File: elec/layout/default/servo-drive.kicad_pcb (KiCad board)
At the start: 4 copper layers, 37.6 x 39.9 mm, 139 parts, among them U37 8Mhz

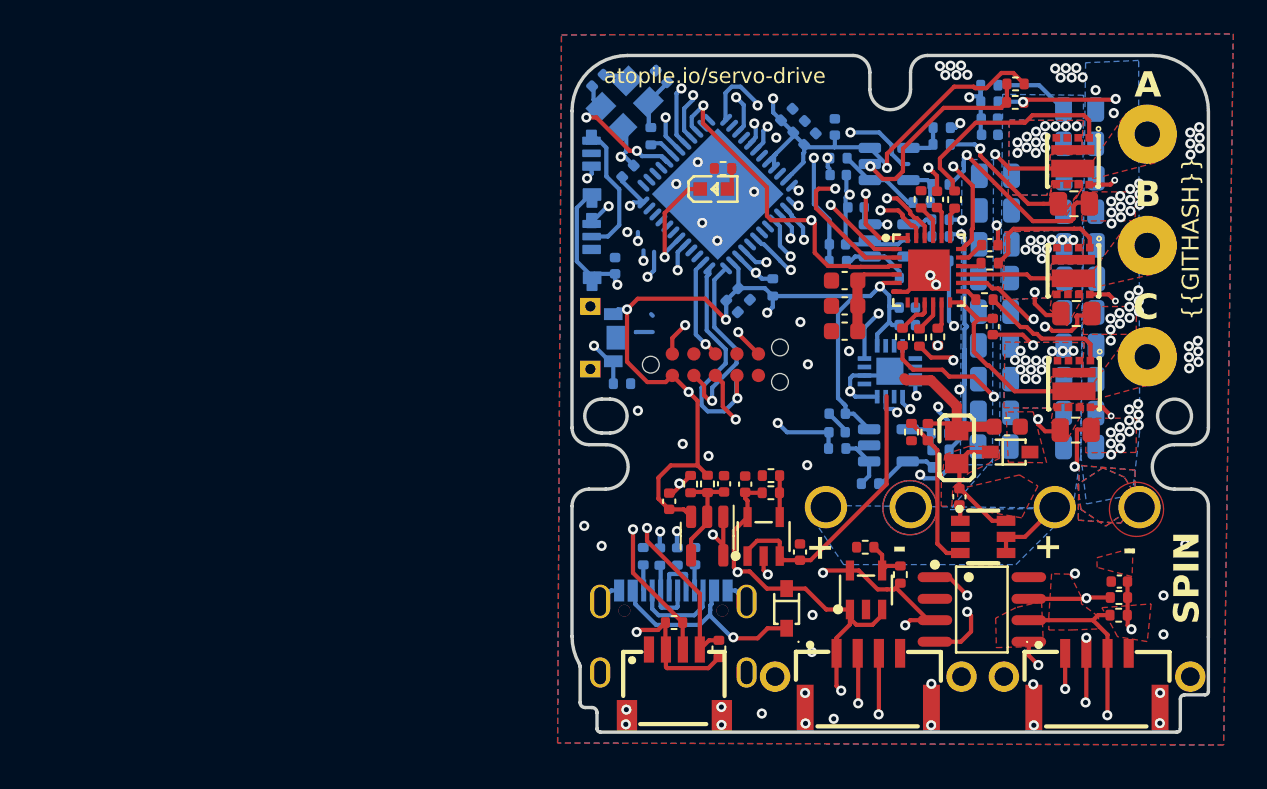
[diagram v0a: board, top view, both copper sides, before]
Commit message: moving layout to correct folder
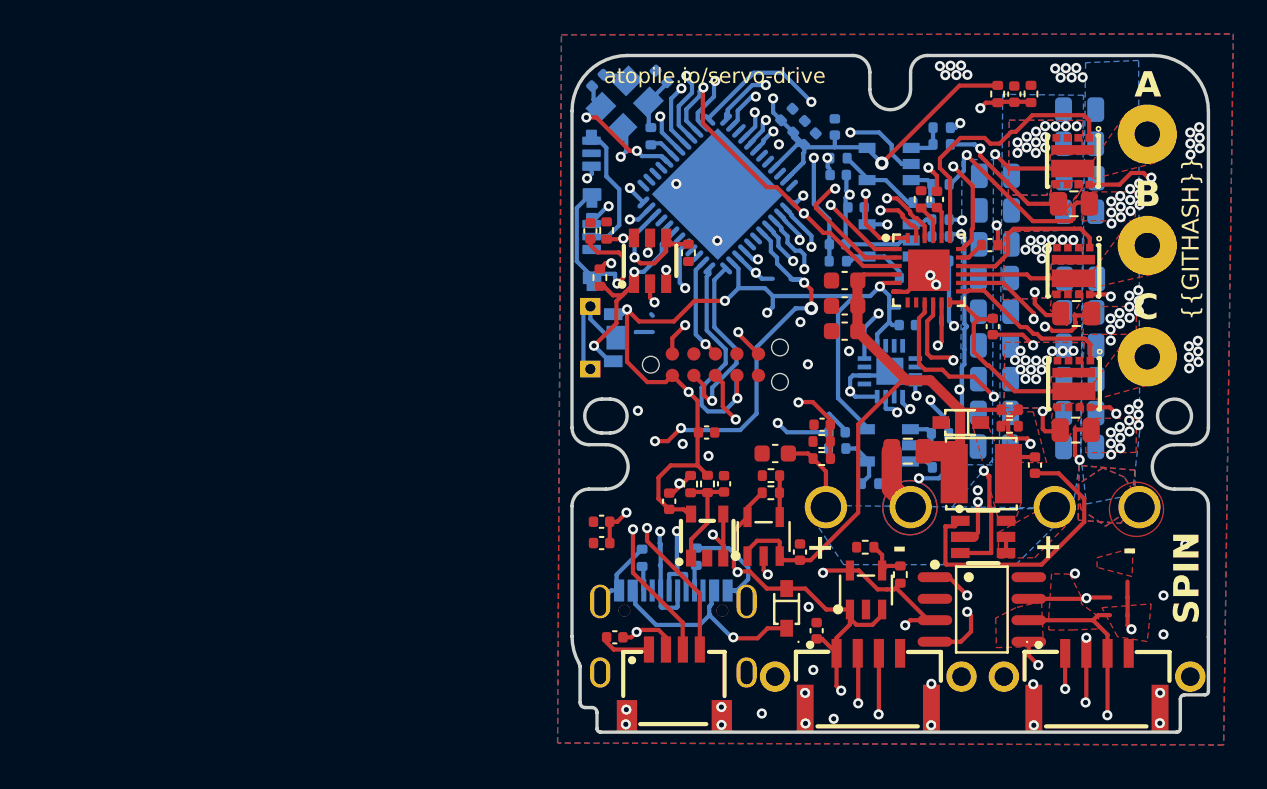
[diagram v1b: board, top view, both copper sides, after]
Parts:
- removed C46: 1uF, Capacitor_SMD:C_0402_1005Metric
- removed C52: 100nF, Capacitor_SMD:C_0402_1005Metric
- removed R23: 60R, Resistor_SMD:R_0402_1005Metric
- removed R24: 1k, Resistor_SMD:R_0402_1005Metric
- removed R27: 10kOhm, Resistor_SMD:R_0402_1005Metric
- removed R28: 1kOhm, Resistor_SMD:R_0402_1005Metric
- removed R32, R33, R34, R35, R36, R37: 10Ohm, Resistor_SMD:R_0402_1005Metric
- removed R39, R40: , Resistor_SMD:R_0402_1005Metric
- C1, C16, C41, C43, C45, C5: value 1uF -> 25V 1uF X5R ±10% 0402 Multilayer Ceramic Capacitors MLCC - SMD/SMT ROHS; footprint Capacitor_SMD:C_0402_1005Metric -> lib:C0402
- C10, C11, C12: value 2200pf -> 50V 2.2nF X7R ±10% 0402 Multilayer Ceramic Capacitors MLCC - SMD/SMT ROHS; footprint Capacitor_SMD:C_0402_1005Metric -> lib:C0402
- C13, C17, C51: value 100nF -> 16V 100nF X7R ±10% 0402 Multilayer Ceramic Capacitors MLCC - SMD/SMT ROHS; footprint Capacitor_SMD:C_0402_1005Metric -> lib:C0402
- C14, C15, C34: value 100nF -> 25V 1uF X5R ±10% 0402 Multilayer Ceramic Capacitors MLCC - SMD/SMT ROHS; footprint Capacitor_SMD:C_0402_1005Metric -> lib:C0402; moved to F.Cu
- C18, C19: value 1uF -> 16V 100nF X7R ±10% 0402 Multilayer Ceramic Capacitors MLCC - SMD/SMT ROHS; footprint Capacitor_SMD:C_0402_1005Metric -> lib:C0402; moved to F.Cu
- C2, C40: value 1uF -> 16V 100nF X7R ±10% 0402 Multilayer Ceramic Capacitors MLCC - SMD/SMT ROHS; footprint Capacitor_SMD:C_0402_1005Metric -> lib:C0402
- C20, C21, C22, C25, C26, C27, C29, C3, C30, C35, C36, C37, C38, C39, C4, C47, C48, C49, C6: value 10uF -> (none); footprint Capacitor_SMD:C_0805_2012Metric -> lib:C0805
- C23, C31, C32: value 4.7uF -> 16V 4.7uF X5R ±10% 0603 Multilayer Ceramic Capacitors MLCC - SMD/SMT ROHS; footprint Capacitor_SMD:C_0603_1608Metric -> lib:C0603
- C24: value 100nF -> 16V 220nF X7R ±10% 0402 Multilayer Ceramic Capacitors MLCC - SMD/SMT ROHS; footprint Capacitor_SMD:C_0402_1005Metric -> lib:C0402
- C28: value 2.2uF -> 16V 100nF X7R ±10% 0402 Multilayer Ceramic Capacitors MLCC - SMD/SMT ROHS; footprint Capacitor_SMD:C_0805_2012Metric -> lib:C0402; moved to F.Cu
- C33: value (none) -> 25V 1uF X5R ±10% 0402 Multilayer Ceramic Capacitors MLCC - SMD/SMT ROHS; footprint Capacitor_SMD:C_0402_1005Metric -> lib:C0402; moved to F.Cu
- C42, C44: value 20pF -> 50V 20pF C0G ±5% 0402 Multilayer Ceramic Capacitors MLCC - SMD/SMT ROHS; footprint Capacitor_SMD:C_0402_1005Metric -> lib:C0402
- C50, C7: value 100nF -> 25V 1uF X5R ±10% 0402 Multilayer Ceramic Capacitors MLCC - SMD/SMT ROHS; footprint Capacitor_SMD:C_0402_1005Metric -> lib:C0402
- C8: value 4.7uF -> 25V 10uF X5R ±10% 0805 Multilayer Ceramic Capacitors MLCC - SMD/SMT ROHS; footprint Capacitor_SMD:C_0603_1608Metric -> lib:C0805
- C9: value 10nF -> 50V 1uF X5R ±10% 0603 Multilayer Ceramic Capacitors MLCC - SMD/SMT ROHS; footprint Capacitor_SMD:C_0402_1005Metric -> lib:C0603
- R1, R38: value 10k -> 62.5mW Thick Film Resistors ±100ppm/℃ ±1% 10kΩ 0402 Chip Resistor - Surface Mount ROHS; footprint Resistor_SMD:R_0402_1005Metric -> lib:R0402
- R10: value 27R -> 62.5mW Thick Film Resistors ±100ppm/℃ ±1% 27.4kΩ 0402 Chip Resistor - Surface Mount ROHS; footprint Resistor_SMD:R_0402_1005Metric -> lib:R0402; moved to F.Cu
- R11: value 1k5 -> 62.5mW ±1% ±200ppm/℃ 3.01kΩ 0402 Chip Resistor - Surface Mount ROHS; footprint Resistor_SMD:R_0402_1005Metric -> lib:R0402; moved to F.Cu
- R12, R14, R26, R45, R49, R51: value 45k -> 62.5mW Thick Film Resistors ±100ppm/℃ ±1% 47kΩ 0402 Chip Resistor - Surface Mount ROHS; footprint Resistor_SMD:R_0402_1005Metric -> lib:R0402
- R13, R25, R44, R48, R50, R6: value 1k -> 62.5mW Thick Film Resistors ±100ppm/℃ ±1% 1kΩ 0402 Chip Resistor - Surface Mount ROHS; footprint Resistor_SMD:R_0402_1005Metric -> lib:R0402
- R15: value 60R -> 62.5mW Thick Film Resistors ±100ppm/℃ ±1% 10kΩ 0402 Chip Resistor - Surface Mount ROHS; footprint Resistor_SMD:R_0402_1005Metric -> lib:R0402
- R16, R46, R52: value 56R -> 62.5mW ±1% ±200ppm/℃ 73.2Ω 0402 Chip Resistor - Surface Mount ROHS; footprint Resistor_SMD:R_0402_1005Metric -> lib:R0402
- R17: value 18k -> 62.5mW Thick Film Resistors ±100ppm/℃ ±1% 20.5kΩ 0402 Chip Resistor - Surface Mount ROHS; footprint Resistor_SMD:R_0402_1005Metric -> lib:R0402
- R18: value 5.1k -> 62.5mW Thick Film Resistors ±100ppm/℃ ±1% 6.34kΩ 0402 Chip Resistor - Surface Mount ROHS; footprint Resistor_SMD:R_0402_1005Metric -> lib:R0402
- R19: value 5.1k -> 10 +/- 0.1 (1%) kiloohm; footprint Resistor_SMD:R_0402_1005Metric -> lib:R0402; moved to F.Cu
- R2: value 10k -> 62.5mW Thick Film Resistors ±100ppm/℃ ±1% 1kΩ 0402 Chip Resistor - Surface Mount ROHS; footprint Resistor_SMD:R_0402_1005Metric -> lib:R0402
- R20: value 5.1k -> 62.5mW Thick Film Resistors ±100ppm/℃ ±1% 10kΩ 0402 Chip Resistor - Surface Mount ROHS; footprint Resistor_SMD:R_0402_1005Metric -> lib:R0402; moved to F.Cu
- R21: value 18k -> 62.5mW Thick Film Resistors ±100ppm/℃ ±1% 11.5kΩ 0402 Chip Resistor - Surface Mount ROHS; footprint Resistor_SMD:R_0402_1005Metric -> lib:R0402
- R22: value 10k -> 62.5mW Thick Film Resistors ±100ppm/℃ ±1% 6.19kΩ 0402 Chip Resistor - Surface Mount ROHS; footprint Resistor_SMD:R_0402_1005Metric -> lib:R0402
- R29: value 147K -> 62.5mW Thick Film Resistors ±100ppm/℃ ±1% 41.2kΩ 0402 Chip Resistor - Surface Mount ROHS; footprint Resistor_SMD:R_0402_1005Metric -> lib:R0402
- R3: value 10k -> 62.5mW Thick Film Resistors ±100ppm/℃ ±1% 100kΩ 0402 Chip Resistor - Surface Mount ROHS; footprint Resistor_SMD:R_0402_1005Metric -> lib:R0402; moved to F.Cu
- R30: value 10K -> 62.5mW Thick Film Resistors ±100ppm/℃ ±1% 4.32kΩ 0402 Chip Resistor - Surface Mount ROHS; footprint Resistor_SMD:R_0402_1005Metric -> lib:R0402
- R31: value 40.2kOhm -> 62.5mW Thick Film Resistors ±100ppm/℃ ±1% 40.2kΩ 0402 Chip Resistor - Surface Mount ROHS; footprint Resistor_SMD:R_0402_1005Metric -> lib:R0402
- R4, R47, R8: value 3mOhm -> (none); footprint Resistor_SMD:R_0805_2012Metric -> lib:R0805
- R5: value 10k_NTC -> 62.5mW Thick Film Resistors ±100ppm/℃ ±1% 5.1kΩ 0402 Chip Resistor - Surface Mount ROHS; footprint Resistor_SMD:R_0402_1005Metric -> lib:R0402; moved to B.Cu
- R7: value 220 -> 62.5mW Thick Film Resistors ±100ppm/℃ ±1% 220Ω 0402 Chip Resistor - Surface Mount ROHS; footprint Resistor_SMD:R_0402_1005Metric -> lib:R0402
- R9: value 27R -> 62.5mW Thick Film Resistors ±100ppm/℃ ±1% 5.1kΩ 0402 Chip Resistor - Surface Mount ROHS; footprint Resistor_SMD:R_0402_1005Metric -> lib:R0402
- U10: footprint lib:L0805 -> lib:IND-SMD_L4.0-W4.0
- U20, U21, U24, U4: footprint Package_TO_SOT_SMD:SOT-23-5 -> lib:SOT-23-5_L3.0-W1.7-P0.95-LS2.8-BR
- U29: footprint lib:LED0603-RD -> lib:SOT-23-6_L2.9-W1.6-P0.95-LS2.8-BR
- U37: value 8Mhz -> (none)
- moved R19 33.7 mm to (232.0, 84.0)
- moved R5 32.8 mm to (212.3, 111.3), turned to 90 degrees
- moved C33 31.0 mm to (219.4, 115.7), turned to 90 degrees
- moved R15 30.6 mm to (230.1, 84.0), turned to -90 degrees
- moved C34 24.5 mm to (206.0, 92.1), turned to 90 degrees
- moved C18 21.9 mm to (207.5, 116.0), turned to 180 degrees
- moved R2 21.7 mm to (211.8, 93.4), turned to -90 degrees
- moved C9 21.7 mm to (216.9, 105.2)
- moved R20 16.6 mm to (206.6, 94.8), turned to -90 degrees
- moved C14 15.9 mm to (206.7, 110.5), turned to 180 degrees
- moved C15 15.9 mm to (206.7, 109.2), turned to 180 degrees
- moved R10 10.3 mm to (219.7, 105.5), turned to 0 degrees
- moved C28 9.73 mm to (231.1, 84.0), turned to 90 degrees
- moved R11 9.54 mm to (219.7, 104.5), turned to 180 degrees
- moved R3 9.08 mm to (207.0, 92.0), turned to 90 degrees
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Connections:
- net SpinServoNEMA17-a_isense renamed power_stage.phase_a.current_sensor-vcc-1
- net SpinServoNEMA17-b_isense renamed power_stage.phase_b.current_sensor-vcc
- net SpinServoNEMA17-data_out renamed ios.led1-vcc
- net SpinServoNEMA17-miso renamed micro-miso
- net SpinServoNEMA17-mosi renamed micro-mosi
- net SpinServoNEMA17-out_a renamed power_stage.phase_a.half_bridge-vcc-2
- net SpinServoNEMA17-out_b renamed power_stage.phase_b.half_bridge-vcc-2
- net SpinServoNEMA17-out_c renamed power_stage.phase_c.half_bridge-vcc-2
- net SpinServoNEMA17-p3 renamed canl
- net SpinServoNEMA17-phase_a renamed power_stage.phase_a-vcc
- net SpinServoNEMA17-phase_b renamed power_stage.phase_b-vcc
- net SpinServoNEMA17-phase_c renamed power_stage.phase_c-vcc
- net SpinServoNEMA17-sck renamed sck
- net SpinServoNEMA17-vin-1 renamed power_stage-vcc-1
- net _a-gnd-2 renamed power_stage.phase_a.half_bridge-gnd
- net _b-i_in-2 renamed power_stage.phase_b.half_bridge-gnd
- net _c-i_in-2 renamed power_stage.phase_c.half_bridge-gnd
- net _i_sense-in-4 renamed power_stage.phase_a.current_sensor.opamp-gnd
- net _i_sense-in-5 renamed power_stage.phase_b.current_sensor.opamp-gnd
- net _i_sense-in_n-5 renamed power_stage.phase_a.current_sensor.opamp-inverting
- net _i_sense-in_n-6 renamed power_stage.phase_b.current_sensor.opamp-inverting
- net _i_sense-in_p-3 renamed power_stage.phase_a.current_sensor.opamp-non_inverting
- net _i_sense-input-10 renamed power_stage.phase_a.current_sensor.bias_div-vcc
- net _i_sense-input-11 renamed power_stage.phase_a.current_sensor.feedback_div-vcc
- net _i_sense-input-12 renamed power_stage.phase_b.current_sensor.feedback_div-vcc
- net _i_sense-input-13 renamed power_stage.phase_c.current_sensor.bias_div-vcc
- net _i_sense-input-14 renamed power_stage.phase_c.current_sensor.feedback_div-vcc
- net _i_sense-out-1 renamed power_stage.phase_c.current_sensor.opamp-gnd
- net _i_sense-output-6 renamed power_stage.phase_b.current_sensor.opamp-non_inverting
- net _i_sense-output-7 renamed power_stage.phase_c.current_sensor.opamp-non_inverting
- net _i_sense-output-8 renamed power_stage.phase_c.current_sensor.opamp-inverting
- net _i_sense-p1-4 renamed power_stage.phase_b.current_sensor.bias_div-vcc
- net gate_reg-cb-1 renamed cb
- net gate_reg-fb renamed power_supply.buck.feedback_div-out
- net gate_reg-sw-1 renamed sw
- net ldo_3v3-adj-1 renamed power_supply.ldo3V3.feedback_div-out
- net ldo_5v-output renamed power_supply.ldo5V.feedback_div-out
- net led2-data_out-1 renamed ios.led2-vcc
- net micro-PA10-2 renamed micro-vcc-4
- net micro-PA13-1 renamed tms
- net micro-PB10-2 renamed pb10
- net micro-PB7-2 renamed micro.micro-sda
- net micro-PC10-2 renamed pc10
- net micro-PC11-2 renamed pc11
- net micro-PC13-2 renamed pc13
- net micro-PC14_OSC32_IN-2 renamed pc14_osc32_in
- net micro-PC15_OSC32_OUT-2 renamed pc15_osc32_out
- net micro-PF1_OSC_OUT-1 renamed pf1_osc_out
- net micro-VBAT-2 renamed micro.micro.ic-vcc
- net micro-in renamed micro.micro.ic-vcc-1
- net micro-out-1 renamed xout
- net micro-rst renamed reset
- net micro-tck renamed tck
- net micro-tdi-1 renamed tdi
- net micro-tdo-1 renamed tdo
- net power_stage-BSTA renamed power_stage.gate_driver.ic-vcc
- net power_stage-BSTB-1 renamed power_stage.gate_driver.ic-vcc-1
- net power_stage-DT-1 renamed power_stage.gate_driver.ic-vcc-3
- net power_stage-bs-1 renamed power_stage.gate_driver.ic-vcc-2
- net power_stage-i_fb_zero-1 renamed power_stage.phase_a.current_sensor-vcc
- net sensor-a-2 renamed position_sensor.ma732-vcc
- net sensor-b-2 renamed position_sensor.ma732-vcc-1
- net sensor-mgh-2 renamed position_sensor.ma732-vcc-3
- net sensor-mgl-2 renamed mgl
- net sensor-nc-2 renamed n_c
- net sensor-pwm-2 renamed pwm
- net sensor-ssck-2 renamed ssck
- net sensor-ssd-2 renamed ssd
- net usbc-vbus-1 renamed power_supply-vcc
- net vref_1V65-vref_unbuf-2 renamed power_stage.voltage_reference.opamp-non_inverting
- C1 pad 1: SpinServoNEMA17-vin -> power_stage-vcc-2
- C1 pad 2: SpinServoNEMA17-gnd -> power_stage-gnd
- C10 pad 2: SpinServoNEMA17-gnd -> power_stage-gnd
- C11 pad 2: SpinServoNEMA17-gnd -> power_stage-gnd
- C12 pad 1: SpinServoNEMA17-c_isense -> power_stage.phase_c.current_sensor-vcc
- C12 pad 2: SpinServoNEMA17-gnd -> power_stage-gnd
- C13 pad 1: SpinServoNEMA17-vin -> power_stage-vcc-2
- C13 pad 2: SpinServoNEMA17-gnd -> power_stage-gnd
- C14 pad 1: SpinServoNEMA17-vin -> power_supply-vcc-1
- C14 pad 2: SpinServoNEMA17-gnd -> power_stage-gnd
- C15 pad 1: SpinServoNEMA17-vin -> power_supply-vcc-1
- C15 pad 2: SpinServoNEMA17-gnd -> power_stage-gnd
- C16 pad 1: SpinServoNEMA17-p1 -> power_stage-vcc-2
- C16 pad 2: SpinServoNEMA17-gnd -> power_stage-gnd
- C17 pad 1: SpinServoNEMA17-vin -> power_stage-vcc-2
- C17 pad 2: SpinServoNEMA17-gnd -> power_stage-gnd
- C18 pad 1: SpinServoNEMA17-p1 -> power_stage-vcc-2
- C18 pad 2: SpinServoNEMA17-gnd -> power_stage-gnd
- C19 pad 1: SpinServoNEMA17-vin -> micro-vcc-3
- C19 pad 2: SpinServoNEMA17-gnd -> power_stage-gnd
- C2 pad 2: SpinServoNEMA17-gnd -> power_stage-gnd
- C20 pad 1: SpinServoNEMA17-vin-2 -> power_stage-vcc
- C20 pad 2: SpinServoNEMA17-gnd -> power_stage-gnd
- C21 pad 1: SpinServoNEMA17-vin-2 -> power_stage-vcc
- C21 pad 2: SpinServoNEMA17-gnd -> power_stage-gnd
- C22 pad 1: SpinServoNEMA17-vin-2 -> power_stage-vcc
- C22 pad 2: SpinServoNEMA17-gnd -> power_stage-gnd
- C23 pad 2: SpinServoNEMA17-gnd -> power_stage-gnd
- C25 pad 1: SpinServoNEMA17-vin-2 -> power_stage-vcc
- C25 pad 2: SpinServoNEMA17-gnd -> power_stage-gnd
- C26 pad 1: SpinServoNEMA17-vin-2 -> power_stage-vcc
- C26 pad 2: SpinServoNEMA17-gnd -> power_stage-gnd
- C27 pad 1: SpinServoNEMA17-vin-2 -> power_stage-vcc
- C27 pad 2: SpinServoNEMA17-gnd -> power_stage-gnd
- C28 pad 1: SpinServoNEMA17-vin-2 -> micro-vcc-2
- C28 pad 2: SpinServoNEMA17-gnd -> power_stage-gnd
- C29 pad 1: SpinServoNEMA17-vin-2 -> power_stage-vcc
- C29 pad 2: SpinServoNEMA17-gnd -> power_stage-gnd
- C3 pad 1: SpinServoNEMA17-vin-2 -> power_stage-vcc
- C3 pad 2: SpinServoNEMA17-gnd -> power_stage-gnd
- C30 pad 1: SpinServoNEMA17-vin-2 -> power_stage-vcc
- C30 pad 2: SpinServoNEMA17-gnd -> power_stage-gnd
- C31 pad 2: SpinServoNEMA17-gnd -> power_stage-gnd
- C32 pad 2: SpinServoNEMA17-gnd -> power_stage-gnd
- C33 pad 1: SpinServoNEMA17-vin_sense -> power_supply-vcc-1
- C33 pad 2: SpinServoNEMA17-gnd -> power_stage-gnd
- C34 pad 1: SpinServoNEMA17-vin_sense -> power_supply-vcc-1
- C34 pad 2: SpinServoNEMA17-gnd -> power_stage-gnd
- C35 pad 1: SpinServoNEMA17-vin-2 -> power_stage-vcc
- C35 pad 2: SpinServoNEMA17-gnd -> power_stage-gnd
- C36 pad 1: SpinServoNEMA17-vin-2 -> power_stage-vcc
- C36 pad 2: SpinServoNEMA17-gnd -> power_stage-gnd
- C37 pad 1: SpinServoNEMA17-vin-2 -> power_stage-vcc
- C37 pad 2: SpinServoNEMA17-gnd -> power_stage-gnd
- C38 pad 1: SpinServoNEMA17-vin-2 -> power_stage-vcc
- C38 pad 2: SpinServoNEMA17-gnd -> power_stage-gnd
- C39 pad 1: SpinServoNEMA17-vin-2 -> power_stage-vcc
- C39 pad 2: SpinServoNEMA17-gnd -> power_stage-gnd
- C4 pad 1: SpinServoNEMA17-vin-2 -> power_stage-vcc
- C4 pad 2: SpinServoNEMA17-gnd -> power_stage-gnd
- C40 pad 1: SpinServoNEMA17-vin -> power_stage-vcc-2
- C40 pad 2: SpinServoNEMA17-gnd -> power_stage-gnd
- C42 pad 2: SpinServoNEMA17-gnd -> power_stage-gnd
- C44 pad 2: SpinServoNEMA17-gnd -> power_stage-gnd
- C47 pad 1: SpinServoNEMA17-vin-2 -> power_stage-vcc
- C47 pad 2: SpinServoNEMA17-gnd -> power_stage-gnd
- C48 pad 1: SpinServoNEMA17-vin-2 -> power_stage-vcc
- C48 pad 2: SpinServoNEMA17-gnd -> power_stage-gnd
- C49 pad 1: SpinServoNEMA17-vin-2 -> power_stage-vcc
- C49 pad 2: SpinServoNEMA17-gnd -> power_stage-gnd
- C5 pad 2: SpinServoNEMA17-gnd -> power_stage-gnd
- C50 pad 1: SpinServoNEMA17-vin -> power_stage-vcc-2
- C50 pad 2: SpinServoNEMA17-gnd -> power_stage-gnd
- C51 pad 1: SpinServoNEMA17-vin -> power_stage-vcc-2
- C51 pad 2: SpinServoNEMA17-gnd -> power_stage-gnd
- C6 pad 1: SpinServoNEMA17-vin-2 -> power_stage-vcc
- C6 pad 2: SpinServoNEMA17-gnd -> power_stage-gnd
- C7 pad 1: SpinServoNEMA17-vin -> power_stage-vcc-2
- C7 pad 2: SpinServoNEMA17-gnd -> power_stage-gnd
- C8 pad 2: SpinServoNEMA17-gnd -> power_stage-gnd
- C9 pad 1: canbus-v_mid-2 -> power_stage-vcc
- C9 pad 2: SpinServoNEMA17-gnd -> power_stage-gnd
- J1 pad 1: SpinServoNEMA17-gnd -> power_stage-gnd
- J1 pad 2: SpinServoNEMA17-gnd -> power_stage-gnd
- J1 pad 3: SpinServoNEMA17-gnd -> power_stage-gnd
- J1 pad 4: SpinServoNEMA17-gnd -> power_stage-gnd
- J1 pad A1: SpinServoNEMA17-gnd -> power_stage-gnd
- J1 pad A12: SpinServoNEMA17-gnd -> power_stage-gnd
- J1 pad A5: SpinServoNEMA17-cc1 -> cc1
- J1 pad A6: SpinServoNEMA17-dp -> dp
- J1 pad A7: SpinServoNEMA17-dm -> dm
- J1 pad A8: usbc-sbu-1 -> sub1
- J1 pad B1: SpinServoNEMA17-gnd -> power_stage-gnd
- J1 pad B12: SpinServoNEMA17-gnd -> power_stage-gnd
- J1 pad B5: SpinServoNEMA17-cc2 -> cc2
- J1 pad B6: SpinServoNEMA17-dp -> dp
- J1 pad B7: SpinServoNEMA17-dm -> dm
- J1 pad B8: usbc-sbu-1 -> sub2
- R1 pad 1: SpinServoNEMA17-vin -> power_stage-vcc-2
- R10 pad 1: micro-PA11-1 -> power_stage-vcc
- R10 pad 2: SpinServoNEMA17-dm -> micro-vcc-3
- R11 pad 1: micro-PA12-1 -> micro-vcc-3
- R11 pad 2: SpinServoNEMA17-vin -> power_stage-gnd
- R15 pad 1: SpinServoNEMA17-p2 -> power_stage-vcc-2
- R15 pad 2: canbus-v_mid-2 -> micro-vcc-2
- R17 pad 1: SpinServoNEMA17-p1 -> power_supply-vcc-1
- R18 pad 2: SpinServoNEMA17-gnd -> power_stage-gnd
- R19 pad 1: SpinServoNEMA17-cc1 -> micro-vcc-2
- R19 pad 2: SpinServoNEMA17-gnd -> power_stage-gnd
- R2 pad 1: SpinServoNEMA17-vin -> micro.micro-io
- R2 pad 2: SpinServoNEMA17-temp_sense -> power_stage-gnd
- R20 pad 1: SpinServoNEMA17-cc2 -> power_stage-gnd
- R20 pad 2: SpinServoNEMA17-gnd -> micro-vcc-1
- R21 pad 1: SpinServoNEMA17-vin -> power_stage-vcc-2
- R22 pad 2: SpinServoNEMA17-gnd -> power_stage-gnd
- R3 pad 1: SpinServoNEMA17-gnd -> micro.micro-io-1
- R3 pad 2: SpinServoNEMA17-in -> power_stage-gnd
- R30 pad 2: SpinServoNEMA17-gnd -> power_stage-gnd
- R31 pad 2: SpinServoNEMA17-gnd -> power_stage-gnd
- R38 pad 2: SpinServoNEMA17-gnd -> power_stage-gnd
- R4 pad 2: SpinServoNEMA17-gnd -> power_stage-gnd
- R47 pad 2: SpinServoNEMA17-gnd -> power_stage-gnd
- R5 pad 1: SpinServoNEMA17-temp_sense -> cc1
- R5 pad 2: SpinServoNEMA17-gnd -> power_stage-gnd
- R52 pad 2: SpinServoNEMA17-c_isense -> power_stage.phase_c.current_sensor-vcc
- R8 pad 2: SpinServoNEMA17-gnd -> power_stage-gnd
- R9 pad 1: micro-PA12-1 -> cc2
- R9 pad 2: SpinServoNEMA17-dp -> power_stage-gnd
- U1 pad 1: _b-high_gate-2 -> power_stage.phase_b.half_bridge-vcc
- U1 pad 10: SpinServoNEMA17-vin-2 -> power_stage-vcc
- U1 pad 2: SpinServoNEMA17-vin-2 -> power_stage-vcc
- U1 pad 3: SpinServoNEMA17-vin-2 -> power_stage-vcc
- U1 pad 4: SpinServoNEMA17-vin-2 -> power_stage-vcc
- U1 pad 8: _b-low_gate-2 -> power_stage.phase_b.half_bridge-vcc-1
- U11 pad 1: SpinServoNEMA17-in -> micro-vcc-1
- U11 pad 2: SpinServoNEMA17-vin -> power_stage-vcc-2
- U11 pad 3: (no net) -> anchor
- U11 pad 4: (no net) -> anchor
- U12 pad 10: power_stage-GLB-1 -> power_stage.phase_b.half_bridge-vcc-1
- U12 pad 11: power_stage-GLA-1 -> power_stage.phase_a.half_bridge-vcc-1
- U12 pad 13: power_stage-GHC-1 -> power_stage.phase_c.half_bridge-vcc
- U12 pad 16: power_stage-GHB-1 -> power_stage.phase_b.half_bridge-vcc
- U12 pad 19: power_stage-GHA-1 -> power_stage.phase_a.half_bridge-vcc
- U12 pad 25: SpinServoNEMA17-gnd -> power_stage-gnd
- U12 pad 5: SpinServoNEMA17-vin -> power_stage-vcc-2
- U12 pad 6: SpinServoNEMA17-gnd -> power_stage-gnd
- U12 pad 7: drv8300-NC2-2 -> (no net)
- U12 pad 8: drv8300-NC1-2 -> (no net)
- U12 pad 9: power_stage-GLC-1 -> power_stage.phase_c.half_bridge-vcc-1
- U13 pad 11: SpinServoNEMA17-enable -> power_stage.phase_c.current_sensor-vcc
- U13 pad 12: micro-PA4-2 -> micro-vcc-2
- U13 pad 13: SpinServoNEMA17-in -> micro-vcc-3
- U13 pad 14: micro-PA6-2 -> micro.micro-io-1
- U13 pad 15: SpinServoNEMA17-led_pixel -> micro.micro-mosi
- U13 pad 16: micro-PC4-2 -> scl
- U13 pad 19: SpinServoNEMA17-c_isense -> pb2
- U13 pad 20: SpinServoNEMA17-vin -> (no net)
- U13 pad 21: SpinServoNEMA17-vin -> power_stage-vcc-2
- U13 pad 23: SpinServoNEMA17-vin -> power_stage-vcc-2
- U13 pad 24: SpinServoNEMA17-cs -> pb11
- U13 pad 25: SpinServoNEMA17-vin_sense -> cs
- U13 pad 29: micro-PC6-2 -> micro-vcc
- U13 pad 30: micro-PA8-2 -> micro-sda
- U13 pad 31: SpinServoNEMA17-temp_sense -> pa9
- U13 pad 33: micro-PA11-1 -> dm
- U13 pad 34: micro-PA12-1 -> dp
- U13 pad 35: SpinServoNEMA17-vin -> power_stage-vcc-2
- U13 pad 42: micro-PB4 -> micro.micro-miso
- U13 pad 43: micro-rx -> micro-vcc-1
- U13 pad 44: micro-tx -> pb6
- U13 pad 46: SpinServoNEMA17-scl -> micro.micro-io
- U13 pad 47: SpinServoNEMA17-sda -> tx
- U13 pad 48: SpinServoNEMA17-vin -> power_stage-vcc-2
- U13 pad 49: SpinServoNEMA17-gnd -> power_stage-gnd
- U14 pad 1: SpinServoNEMA17-gnd -> power_stage-gnd
- U14 pad 2: SpinServoNEMA17-vin-2 -> power_stage-vcc
- U14 pad 3: (no net) -> power_stage-gnd
- U14 pad 4: (no net) -> power_stage-gnd
- U15 pad 1: SpinServoNEMA17-gnd -> power_stage-gnd
- U15 pad 2: SpinServoNEMA17-vin -> power_stage-vcc-2
- U15 pad 3: SpinServoNEMA17-sda -> micro-sda
- U15 pad 4: SpinServoNEMA17-scl -> scl
- U15 pad 5: (no net) -> power_stage-gnd
- U15 pad 6: (no net) -> power_stage-gnd
- U16 pad 1: SpinServoNEMA17-vin -> power_stage-vcc-2
- U16 pad 3: SpinServoNEMA17-gnd -> power_stage-gnd
- U16 pad 5: SpinServoNEMA17-gnd -> power_stage-gnd
- U18 pad 10: SpinServoNEMA17-gnd -> power_stage-gnd
- U18 pad 13: SpinServoNEMA17-vin -> power_stage-vcc-2
- U18 pad 17: SpinServoNEMA17-gnd -> power_stage-gnd
- U18 pad 3: (no net) -> position_sensor.ma732-vcc-2
- U18 pad 5: SpinServoNEMA17-cs -> cs
- U18 pad 8: SpinServoNEMA17-gnd -> power_stage-gnd
- U19 pad 2: SpinServoNEMA17-gnd -> power_stage-gnd
- U2 pad 1: SpinServoNEMA17-gnd -> power_stage-gnd
- U2 pad 2: SpinServoNEMA17-vin-2 -> power_stage-vcc
- U2 pad 3: (no net) -> power_stage-gnd
- U2 pad 4: (no net) -> power_stage-gnd
- U20 pad 2: SpinServoNEMA17-gnd -> power_stage-gnd
- U20 pad 5: SpinServoNEMA17-vin -> power_stage-vcc-2
- U21 pad 2: SpinServoNEMA17-gnd -> power_stage-gnd
- U21 pad 5: SpinServoNEMA17-vin -> power_stage-vcc-2
- U22 pad 2: SpinServoNEMA17-gnd -> power_stage-gnd
- U22 pad 5: SpinServoNEMA17-p1 -> power_supply-vcc-1
- U23 pad 1: SpinServoNEMA17-p1 -> power_supply-vcc-1
- U23 pad 2: SpinServoNEMA17-gnd -> power_stage-gnd
- U23 pad 3: SpinServoNEMA17-p1 -> power_supply-vcc-1
- U23 pad 5: SpinServoNEMA17-vin -> power_stage-vcc-2
- U24 pad 2: SpinServoNEMA17-gnd -> power_stage-gnd
- U24 pad 5: SpinServoNEMA17-vin -> power_stage-vcc-2
- U25 pad 1: micro-tx -> tx
- U25 pad 2: SpinServoNEMA17-gnd -> power_stage-gnd
- U25 pad 3: SpinServoNEMA17-vin -> power_stage-vcc-2
- U25 pad 4: micro-rx -> rx
- U25 pad 5: canbus-v_mid-2 -> vref
- U25 pad 7: SpinServoNEMA17-p2 -> canh
- U25 pad 8: SpinServoNEMA17-gnd -> power_stage-gnd
- U26 pad 1: SpinServoNEMA17-p1 -> power_supply-vcc-1
- U26 pad 2: SpinServoNEMA17-p2 -> canh
- U26 pad 4: SpinServoNEMA17-gnd -> power_stage-gnd
- U26 pad 5: (no net) -> power_stage-gnd
- U26 pad 6: (no net) -> power_stage-gnd
- U27 pad 1: SpinServoNEMA17-p1 -> power_supply-vcc-1
- U27 pad 2: SpinServoNEMA17-p2 -> canh
- U27 pad 4: SpinServoNEMA17-gnd -> power_stage-gnd
- U27 pad 5: (no net) -> power_stage-gnd
- U27 pad 6: (no net) -> power_stage-gnd
- U28 pad 1: _a-high_gate-2 -> power_stage.phase_a.half_bridge-vcc
- U28 pad 10: SpinServoNEMA17-vin-2 -> power_stage-vcc
- U28 pad 2: SpinServoNEMA17-vin-2 -> power_stage-vcc
- U28 pad 3: SpinServoNEMA17-vin-2 -> power_stage-vcc
- U28 pad 4: SpinServoNEMA17-vin-2 -> power_stage-vcc
- U28 pad 8: _a-low_gate-2 -> power_stage.phase_a.half_bridge-vcc-1
- U29 pad 1: micro-PB4 -> micro-vcc-1
- U29 pad 2: debug_led_1-A-2 -> power_stage-gnd
- U3 pad 1: _c-high_gate-2 -> power_stage.phase_c.half_bridge-vcc
- U3 pad 10: SpinServoNEMA17-vin-2 -> power_stage-vcc
- U3 pad 2: SpinServoNEMA17-vin-2 -> power_stage-vcc
- U3 pad 3: SpinServoNEMA17-vin-2 -> power_stage-vcc
- U3 pad 4: SpinServoNEMA17-vin-2 -> power_stage-vcc
- U3 pad 8: _c-low_gate-2 -> power_stage.phase_c.half_bridge-vcc-1
- U30 pad 1: SpinServoNEMA17-p1 -> power_supply-vcc-1
- U32 pad 1: SpinServoNEMA17-p1 -> power_supply-vcc-1
- U32 pad 2: SpinServoNEMA17-gnd -> power_stage-gnd
- U33 pad 2: SpinServoNEMA17-gnd -> power_stage-gnd
- U35 pad 2: SpinServoNEMA17-gnd -> power_stage-gnd
- U36 pad 2: SpinServoNEMA17-gnd -> power_stage-gnd
- U37 pad 2: SpinServoNEMA17-gnd -> power_stage-gnd
- U37 pad 4: SpinServoNEMA17-gnd -> power_stage-gnd
- U4 pad 2: SpinServoNEMA17-gnd -> power_stage-gnd
- U4 pad 5: SpinServoNEMA17-vin -> power_stage-vcc-2
- U5 pad 1: SpinServoNEMA17-p1 -> power_supply-vcc-1
- U5 pad 2: SpinServoNEMA17-gnd -> power_stage-gnd
- U5 pad 4: SpinServoNEMA17-led_pixel -> micro-vcc
- U6 pad 2: SpinServoNEMA17-gnd -> power_stage-gnd
- U6 pad 4: SpinServoNEMA17-vin-2 -> power_stage-vcc
- U6 pad 5: SpinServoNEMA17-vin-2 -> power_stage-vcc
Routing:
- net SpinServoNEMA17-vin: track 114.6 -> 0.00 mm, vias 13 -> 0
- net power_stage-vcc-2: track 0.00 -> 111.3 mm, vias 0 -> 15
- net power_supply-vcc-1: track 0.00 -> 77.8 mm, vias 0 -> 5
- net SpinServoNEMA17-p1: track 70.9 -> 0.00 mm, vias 4 -> 0
- net power_stage-gnd: track 0.00 -> 56.3 mm, vias 0 -> 88
- net SpinServoNEMA17-gnd: track 44.5 -> 0.00 mm, vias 106 -> 0
- net tx: track 0.00 -> 38.2 mm, vias 0 -> 2
- net scl: track 0.00 -> 37.5 mm, vias 0 -> 2
- net micro-sda: track 0.00 -> 36.5 mm, vias 0 -> 5
- net micro-rx: track 35.8 -> 0.00 mm, vias 2 -> 0
- net rx: track 0.00 -> 34.9 mm, vias 0 -> 2
- net micro-tx: track 33.9 -> 0.00 mm, vias 2 -> 0
- net SpinServoNEMA17-in: track 32.4 -> 0.00 mm, vias 2 -> 0
- net power_stage.phase_c.current_sensor-vcc: track 0.00 -> 30.7 mm, vias 0 -> 3
- net SpinServoNEMA17-scl: track 29.6 -> 0.00 mm, vias 2 -> 0
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- added copper zone on B.Cu, net power_stage-gnd
- added copper zone on F.Cu, net power_stage-gnd
- added copper zone on In1.Cu, net power_stage-gnd
- added copper zone on In2.Cu, net power_stage-gnd
- added copper zone on B.Cu, net power_stage-vcc
- added copper zone on F.Cu, net power_stage-vcc
- added copper zone on In1.Cu, net power_stage-vcc
- added copper zone on In2.Cu, net power_stage-vcc
- added copper zone on In2.Cu, net power_stage-vcc-2
- removed copper zone on B.Cu, net SpinServoNEMA17-gnd
- removed copper zone on F.Cu, net SpinServoNEMA17-gnd
- removed copper zone on In1.Cu, net SpinServoNEMA17-gnd
- removed copper zone on In2.Cu, net SpinServoNEMA17-gnd
- removed copper zone on In2.Cu, net SpinServoNEMA17-vin
- removed copper zone on B.Cu, net SpinServoNEMA17-vin-2
- removed copper zone on F.Cu, net SpinServoNEMA17-vin-2
- removed copper zone on In1.Cu, net SpinServoNEMA17-vin-2
- removed copper zone on In2.Cu, net SpinServoNEMA17-vin-2

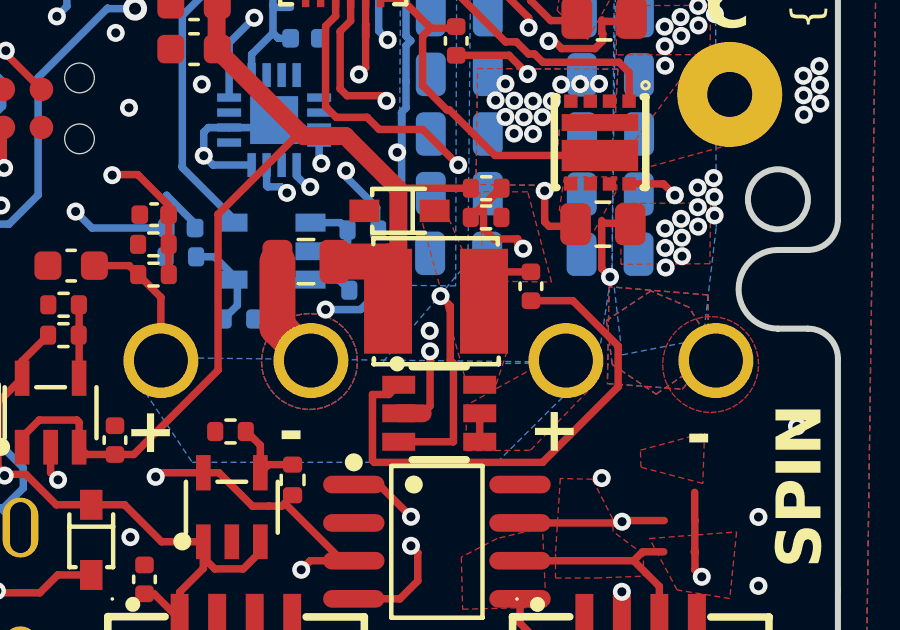
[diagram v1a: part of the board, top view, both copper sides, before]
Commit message: fix net short issue
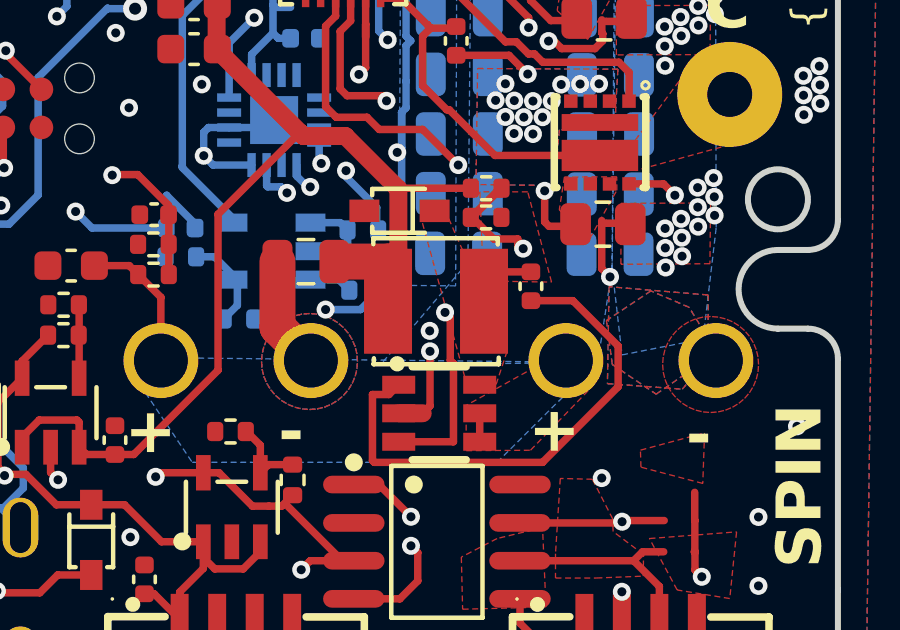
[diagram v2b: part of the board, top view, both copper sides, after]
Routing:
- net power_supply.buck.feedback_div-out: track 29.2 -> 14.9 mm, vias 4 -> 2
- net power_stage.phase_c.current_sensor.feedback_div-vcc: track 0.00 -> 14.0 mm, vias 0 -> 2

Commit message: added 3D step models
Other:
- board text added: "PCB3D_BR_servo-drive"
- board text added: "PCB3D_TL_servo-drive"
